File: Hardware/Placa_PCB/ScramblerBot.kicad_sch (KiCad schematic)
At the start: 0 parts

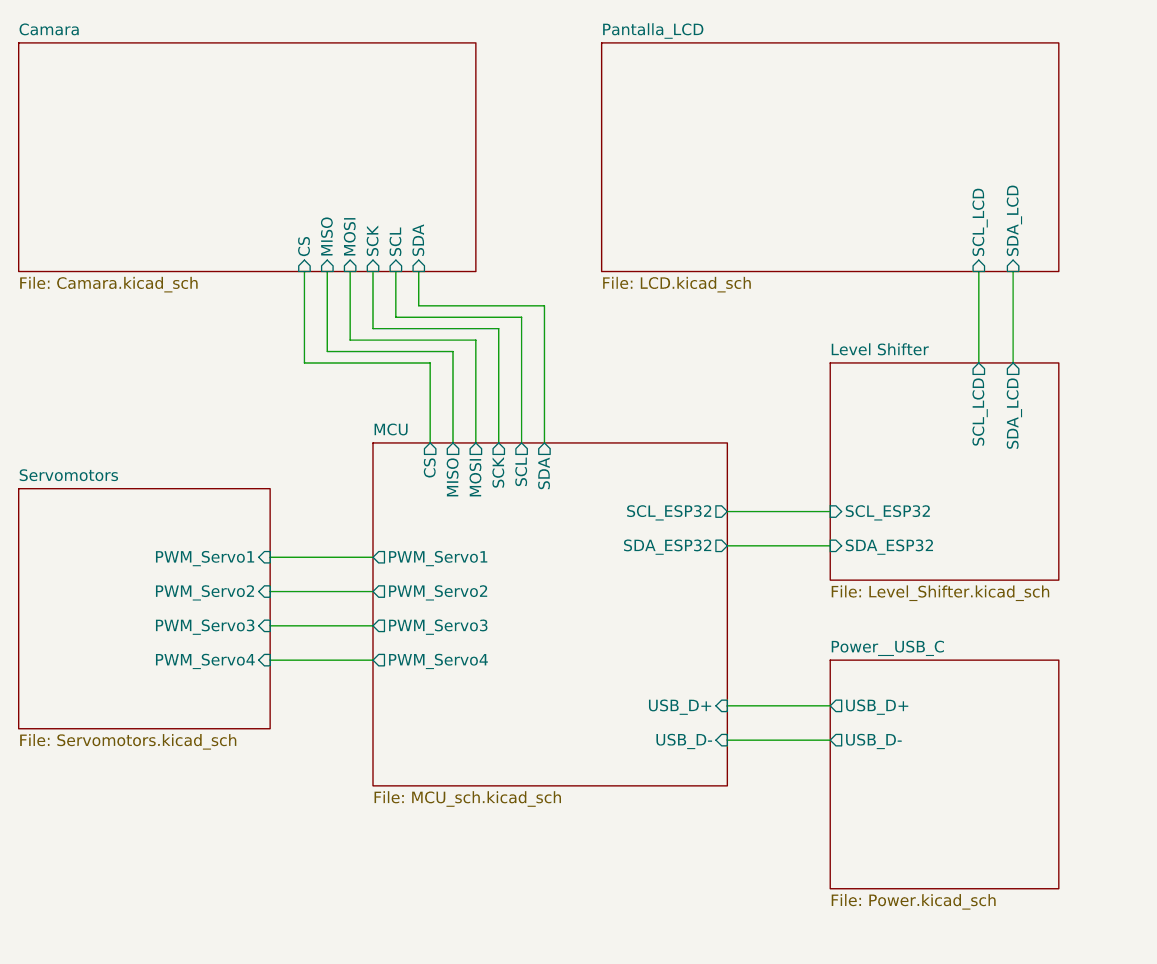
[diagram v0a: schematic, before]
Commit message: Agregando Level Shifter al PWM del Servo
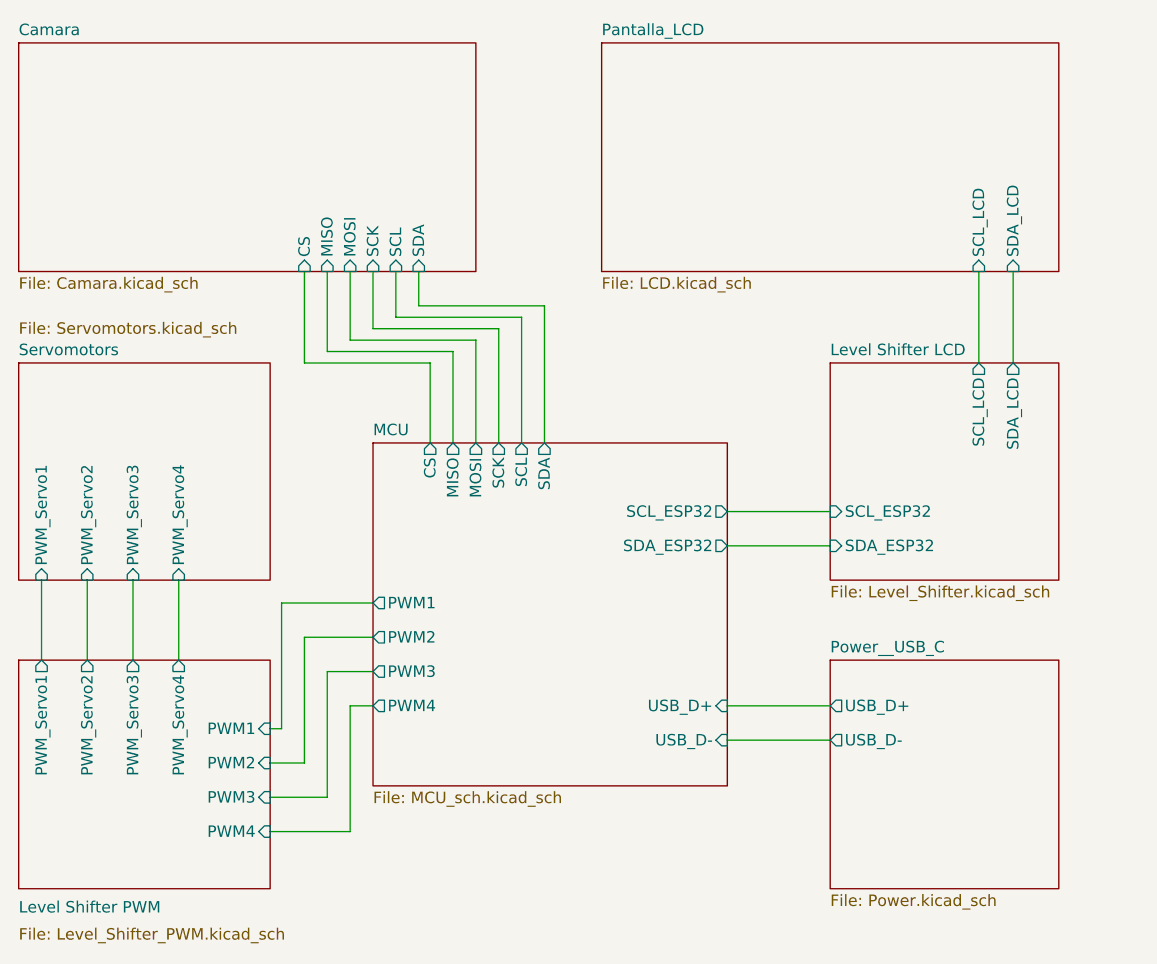
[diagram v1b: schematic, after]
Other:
- sheet Level Shifter renamed Level Shifter LCD
- added sheet Level Shifter PWM (Level_Shifter_PWM.kicad_sch)
- sheet MCU ports: added PWM1, PWM2, PWM3, PWM4; removed PWM_Servo1, PWM_Servo2, PWM_Servo3, PWM_Servo4

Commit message: Agregando MCU al esquematico
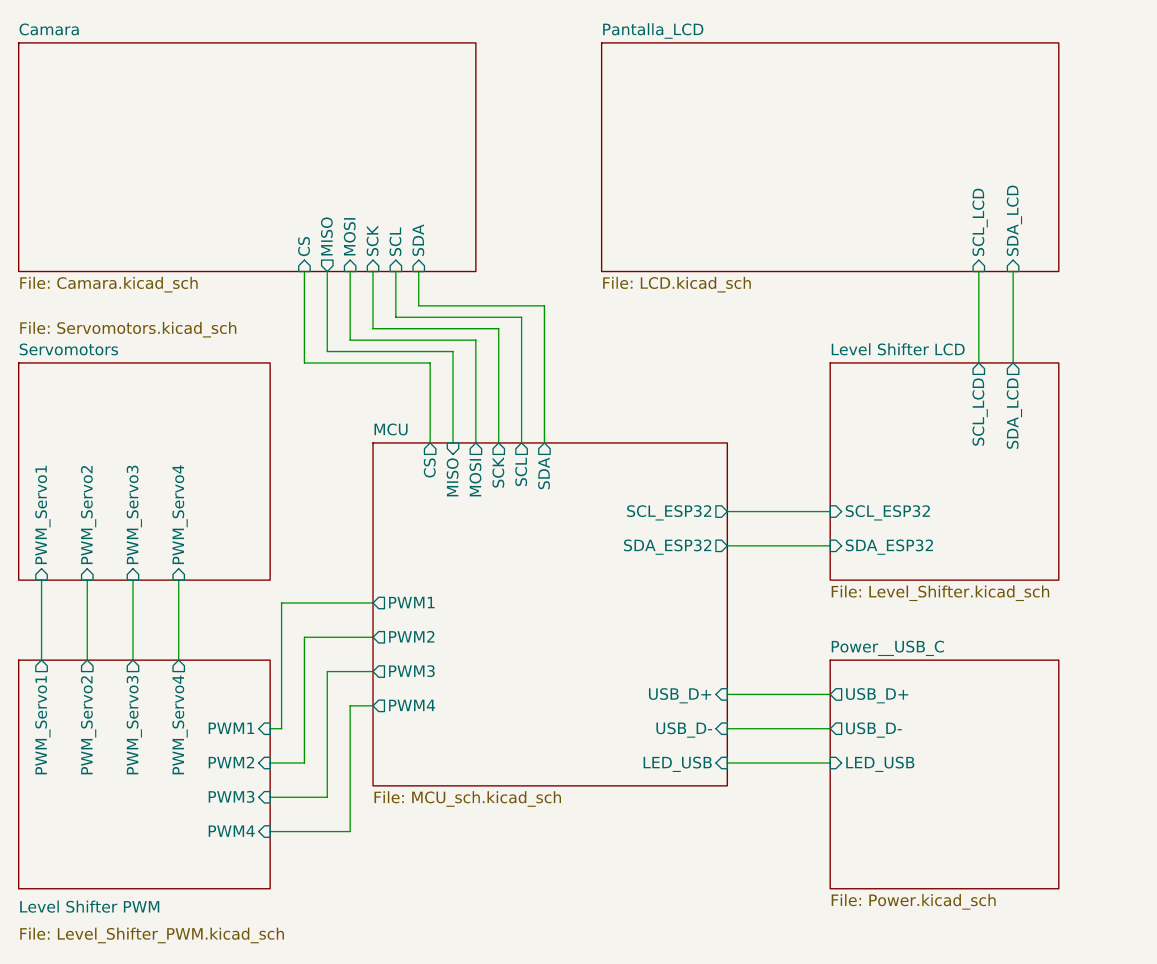
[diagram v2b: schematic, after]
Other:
- sheet MCU ports: added LED_USB; removed none
- sheet Power__USB_C ports: added LED_USB; removed none
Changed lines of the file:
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@@
+	(wire
+		(pts
+			(xy 176.53 120.65) (xy 187.96 120.65)
+		)
+		(stroke
+			(width 0)
+			(type default)
+		)
+	)
 	(wire
 		(pts
@@
 	(wire
 		(pts
+			(xy 176.53 116.84) (xy 187.96 116.84)
+		)
+		(stroke
+			(width 0)
+			(type default)
+		)
+	)
+	(wire
+		(pts
 			(xy 137.16 76.2) (xy 151.13 76.2)
 		)
@@
 	(wire
 		(pts
+			(xy 176.53 124.46) (xy 187.96 124.46)
+		)
+		(stroke
+			(width 0)
+			(type default)
+		)
+	)
+	(wire
+		(pts
 			(xy 132.08 69.85) (xy 132.08 78.74)
 		)
@@
 	(wire
 		(pts
-			(xy 176.53 118.11) (xy 187.96 118.11)
-		)
-		(stroke
-			(width 0)
-			(type default)
-		)
-	)
-	(wire
-		(pts
 			(xy 129.54 124.46) (xy 129.54 110.49)
 		)
@@
 		(pts
 			(xy 132.08 78.74) (xy 146.05 78.74)
-		)
-		(stroke
-			(width 0)
-			(type default)
-		)
-	)
-	(wire
-		(pts
-			(xy 176.53 121.92) (xy 187.96 121.92)
 		)
 		(stroke
@@
 			)
 		)
-		(pin "MISO" input
-			(at 132.08 69.85 270)
-			(effects
-				(font
-					(size 1.27 1.27)
-				)
-				(justify left)
-			)
-		)
 		(pin "MOSI" input
 			(at 134.62 69.85 270)
@@
 		(pin "SCL" input
 			(at 139.7 69.85 270)
+			(effects
+				(font
+					(size 1.27 1.27)
+				)
+				(justify left)
+			)
+		)
+		(pin "MISO" output
+			(at 132.08 69.85 270)
 			(effects
 				(font
@@
 			)
 		)
-		(pin "MISO" output
-			(at 146.05 88.9 90)
+		(pin "SCK" output
+			(at 151.13 88.9 90)
+			(effects
+				(font
+					(size 1.27 1.27)
+				)
+				(justify right)
+			)
+		)
+		(pin "SCL" output
+			(at 153.67 88.9 90)
+			(effects
+				(font
+					(size 1.27 1.27)
+				)
+				(justify right)
+			)
+		)
+		(pin "SCL_ESP32" output
+			(at 176.53 96.52 0)
+			(effects
+				(font
+					(size 1.27 1.27)
+				)
+				(justify right)
+			)
+		)
+		(pin "SDA" output
+			(at 156.21 88.9 90)
+			(effects
+				(font
+					(size 1.27 1.27)
+				)
+				(justify right)
+			)
+		)
+		(pin "SDA_ESP32" output
+			(at 176.53 100.33 0)
+			(effects
+				(font
+					(size 1.27 1.27)
+				)
+				(justify right)
+			)
+		)
+		(pin "USB_D+" input
+			(at 176.53 116.84 0)
+			(effects
+				(font
+					(size 1.27 1.27)
+				)
+				(justify right)
+			)
+		)
+		(pin "USB_D-" input
+			(at 176.53 120.65 0)
+			(effects
+				(font
+					(size 1.27 1.27)
+				)
+				(justify right)
+			)
+		)
+		(pin "PWM1" output
+			(at 137.16 106.68 180)
+			(effects
+				(font
+					(size 1.27 1.27)
+				)
+				(justify left)
+			)
+		)
+		(pin "PWM2" output
+			(at 137.16 110.49 180)
+			(effects
+				(font
+					(size 1.27 1.27)
+				)
+				(justify left)
+			)
+		)
+		(pin "PWM3" output
+			(at 137.16 114.3 180)
+			(effects
+				(font
+					(size 1.27 1.27)
+				)
+				(justify left)
+			)
+		)
+		(pin "PWM4" output
+			(at 137.16 118.11 180)
+			(effects
+				(font
+					(size 1.27 1.27)
+				)
+				(justify left)
+			)
+		)
+		(pin "LED_USB" input
+			(at 176.53 124.46 0)
 			(effects
 				(font
@@
 			)
 		)
-		(pin "SCK" output
-			(at 151.13 88.9 90)
-			(effects
-				(font
-					(size 1.27 1.27)
-				)
-				(justify right)
-			)
-		)
-		(pin "SCL" output
-			(at 153.67 88.9 90)
-			(effects
-				(font
-					(size 1.27 1.27)
-				)
-				(justify right)
-			)
-		)
-		(pin "SCL_ESP32" output
-			(at 176.53 96.52 0)
-			(effects
-				(font
-					(size 1.27 1.27)
-				)
-				(justify right)
-			)
-		)
-		(pin "SDA" output
-			(at 156.21 88.9 90)
-			(effects
-				(font
-					(size 1.27 1.27)
-				)
-				(justify right)
-			)
-		)
-		(pin "SDA_ESP32" output
-			(at 176.53 100.33 0)
-			(effects
-				(font
-					(size 1.27 1.27)
-				)
-				(justify right)
-			)
-		)
-		(pin "USB_D+" input
-			(at 176.53 118.11 0)
-			(effects
-				(font
-					(size 1.27 1.27)
-				)
-				(justify right)
-			)
-		)
-		(pin "USB_D-" input
-			(at 176.53 121.92 0)
-			(effects
-				(font
-					(size 1.27 1.27)
-				)
-				(justify right)
-			)
-		)
-		(pin "PWM1" output
-			(at 137.16 106.68 180)
-			(effects
-				(font
-					(size 1.27 1.27)
-				)
-				(justify left)
-			)
-		)
-		(pin "PWM2" output
-			(at 137.16 110.49 180)
-			(effects
-				(font
-					(size 1.27 1.27)
-				)
-				(justify left)
-			)
-		)
-		(pin "PWM3" output
-			(at 137.16 114.3 180)
-			(effects
-				(font
-					(size 1.27 1.27)
-				)
-				(justify left)
-			)
-		)
-		(pin "PWM4" output
-			(at 137.16 118.11 180)
-			(effects
-				(font
-					(size 1.27 1.27)
-				)
-				(justify left)
+		(pin "MISO" input
+			(at 146.05 88.9 90)
+			(effects
+				(font
+					(size 1.27 1.27)
+				)
+				(justify right)
 			)
 		)
@@
 		)
 		(pin "USB_D+" output
-			(at 187.96 118.11 180)
+			(at 187.96 116.84 180)
 			(effects
 				(font
@@
 		)
 		(pin "USB_D-" output
-			(at 187.96 121.92 180)
-			(effects
-				(font
+			(at 187.96 120.65 180)
+			(effects
+				(font
+					(size 1.27 1.27)
+				)
+				(justify left)
+			)
+		)
+		(pin "LED_USB" input
+			(at 187.96 124.46 180)
+			(effects
+				(font
